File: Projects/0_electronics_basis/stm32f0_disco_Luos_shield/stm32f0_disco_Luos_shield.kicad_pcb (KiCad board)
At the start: 2 copper layers, 55.9 x 99.1 mm, 20 parts, among them J1 DF11-8DP-2DS(24), J2 DF11-8DP-2DS(24), J3 Header6Contacts, J4 Header6Contacts, J5 Discovery_Socket, J6 Header5Contacts, U1 ST3485ECDR

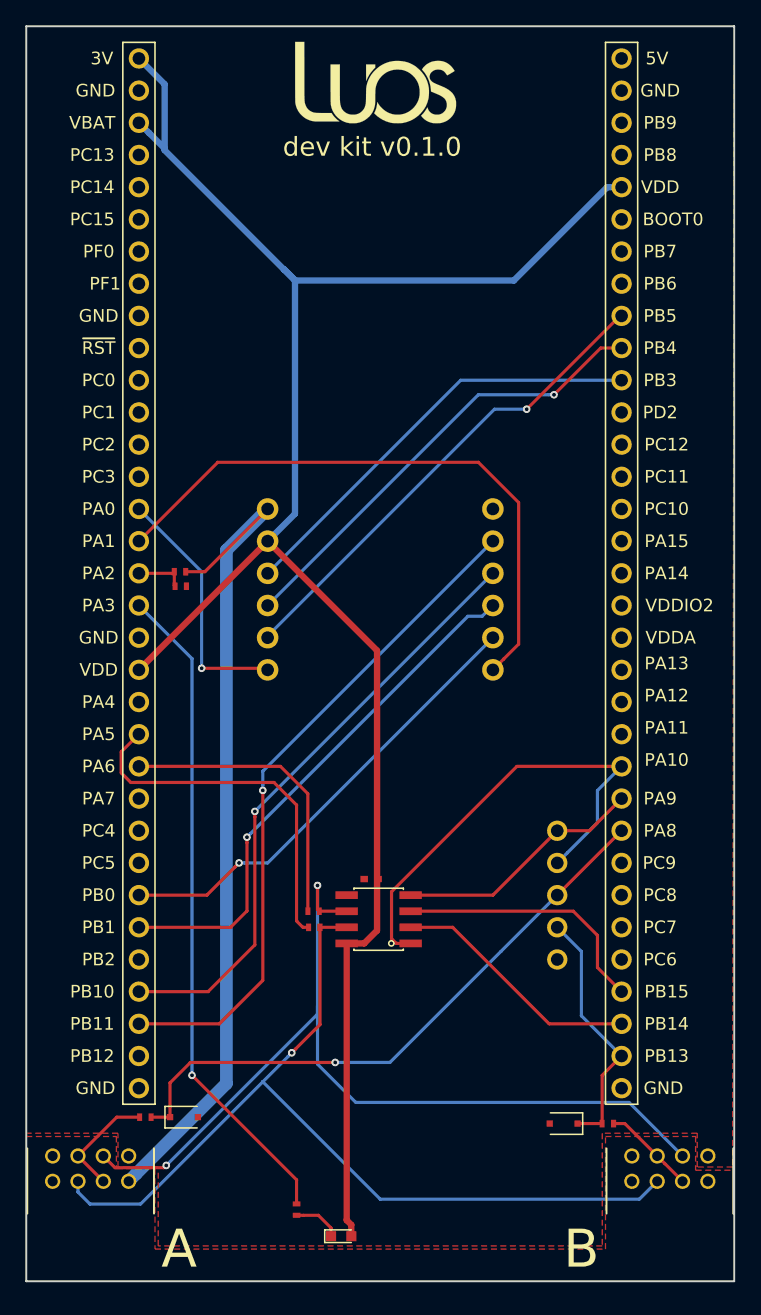
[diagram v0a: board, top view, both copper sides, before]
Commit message: change board kicad for project : Braekout board Luos Kit DC motor Servo
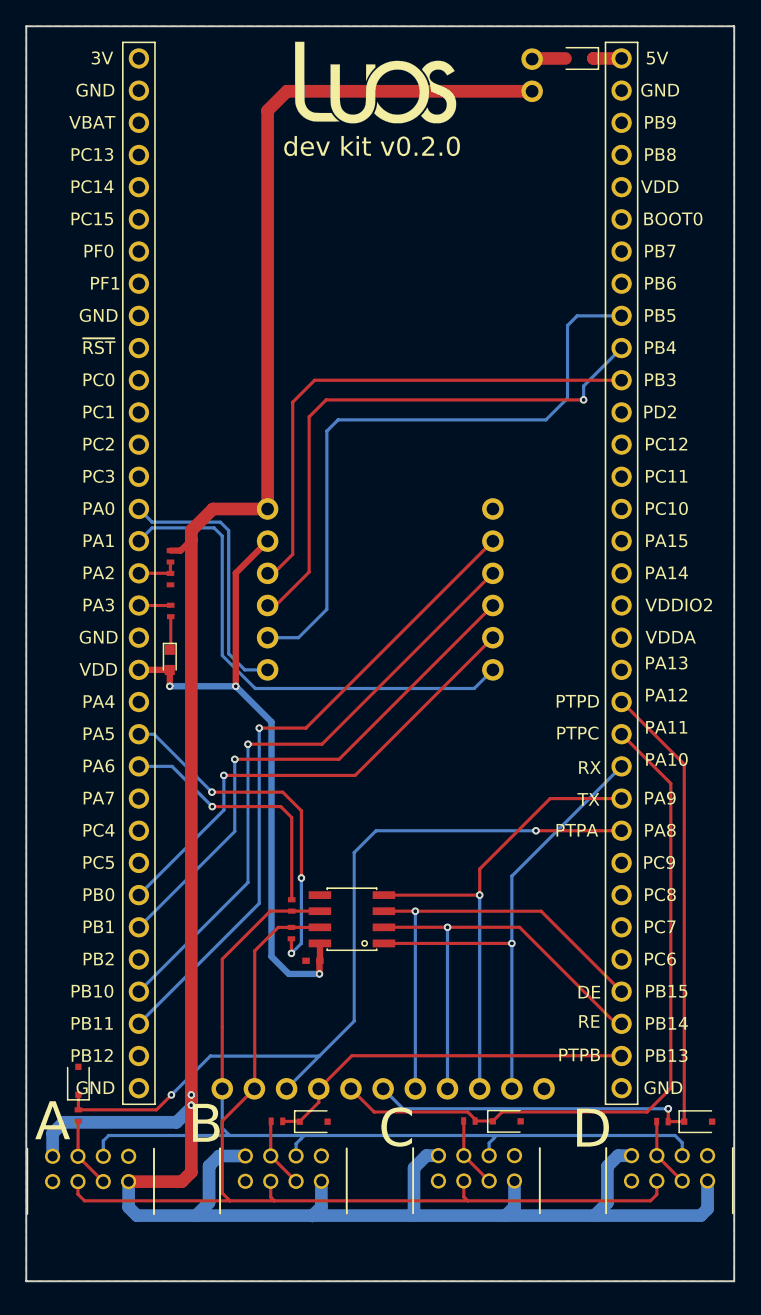
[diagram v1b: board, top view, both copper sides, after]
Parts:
- removed the D2 at (55.9, 111.7)
- removed the J5 at (41.4, 68.3)
- removed the J6 at (55.4, 93.7)
- added D1: D_Zener, Common_Footprint:D_SOD-323F, F.Cu at (17.6, 108.3)
- added D3: D_Zener, Common_Footprint:D_SOD-323F, F.Cu at (51.4, 111.5)
- added D4: D_Zener, Common_Footprint:D_SOD-323F, F.Cu at (66.5, 111.5)
- added D6: SMLE13BC8TT86, Common_Footprint:LED_0603, F.Cu at (24.8, 75.1)
- added J3: DF11-8DP-2DS(24), Common_Footprint:DF11-8DP-2DS(24), F.Cu at (49.0, 115.2)
- added J4: DF11-8DP-2DS, Common_Footprint:DF11-8DP-2DS(24), F.Cu at (64.3, 115.2)
- added J7: Discovery_Socket, Common_Footprint:Discovery_Socket, B.Cu at (41.4, 68.3)
- added J8: Header11Contacts, Common_Footprint:826926-11, B.Cu at (42.9, 109.0)
- added J9: Header2Contacts, Common_Footprint:826926-2, B.Cu at (53.4, 27.7)
- added R3: 100, Common_Footprint:R_0402_NoSilk, F.Cu at (48.5, 111.5)
- added R4: 100, Common_Footprint:R_0402_NoSilk, F.Cu at (63.7, 111.5)
- D5: value SMLE13BC8TT86 -> DIODE; footprint Common_Footprint:LED_0603 -> Common_Footprint:D_SOD-323F
- J1: value DF11-8DP-2DS(24) -> DF11-8DP-2DS
- moved D5 94.8 mm to (57.2, 27.6), turned to 180 degrees
- moved R9 48.3 mm to (24.9, 71.2)
- moved J1 45.7 mm to (18.6, 115.3)
- moved R1 41.8 mm to (17.6, 111.1), turned to 270 degrees
- moved J2 15.2 mm to (33.8, 115.3)
- moved R2 10.4 mm to (33.3, 111.5)
- moved D2 10.2 mm to (36.2, 111.5)
- moved C1 7.92 mm to (36.1, 98.8)
- moved U1 2.11 mm to (39.2, 95.6)
- moved R5 1.86 mm to (34.4, 96.7), turned to 90 degrees
- moved R6 1.78 mm to (34.5, 94.5), turned to 90 degrees
- moved R7 1.43 mm to (24.9, 66.9), turned to 90 degrees
- moved R8 0.99 mm to (24.9, 68.7), turned to 90 degrees
- renumbered C7 to C1, D3 to D2, J3 to J5, J4 to J6, R6 to R5, R7 to R6, R11 to R7, R12 to R8, R13 to R9
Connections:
- D2 pad 1: /PTPA -> /PTPB
- D5 pad 1: Net-(D5-Pad1) -> +5VP
- D5 pad 2: +3V3 -> Net-(D5-Pad2)
- J1 pad 3: /PTPB_PRO -> /PTPA_PRO
- J1 pad 6: /PTPB_PRO -> /PTPA_PRO
- J2 pad 3: /PTPA_PRO -> /PTPB_PRO
- J2 pad 6: /PTPA_PRO -> /PTPB_PRO
- R1 pad 1: /PTPB -> /PTPA
- R1 pad 2: /PTPB_PRO -> /PTPA_PRO
- R2 pad 1: /PTPA -> /PTPB
- R2 pad 2: /PTPA_PRO -> /PTPB_PRO
- R9 pad 1: Net-(D5-Pad1) -> Net-(D6-Pad1)
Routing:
- net /Vin: track 66.1 -> 208.9 mm, vias 0 -> 2
- net +3V3: track 151.8 -> 50.8 mm, vias 0 -> 3
- net /PTPD: track 0.00 -> 60.6 mm, vias 0 -> 1
- net /PTPC: track 0.00 -> 57.0 mm
- net Net-(J7-Pad49): track 52.4 -> 2.52 mm, vias 1 -> 0
- net /TxD: track 19.8 -> 38.4 mm, vias 0 -> 1
- net /PTPA: track 48.1 -> 64.7 mm, vias 1 -> 2
- net /RE: track 19.8 -> 34.7 mm, vias 0 -> 1
- net /DE: track 20.8 -> 35.4 mm, vias 0 -> 1
- net /MOSI/SD: track 38.5 -> 50.3 mm, vias 1 -> 0
- net /PTPB: track 20.2 -> 29.6 mm
- net /TIM2.2/ADC1: track 47.9 -> 39.8 mm
- net /MISO/MCK: track 36.4 -> 44.2 mm
- net /SCK/CK: track 34.3 -> 41.3 mm
- net /B_RS_485_P: track 71.6 -> 78.6 mm, vias 1 -> 0
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- removed copper zone on F.Cu, net /Vin
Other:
- net class ALIM added: clearance 0.508, trace_width 1, via_dia 0.6, via_drill 0.3
- board text added: "C"
- board text added: "D"
- board text added: "DE"
- board text added: "PTPC"
- board text added: "PTPD"
- board text added: "RE"
- board text added: "RX"
- board text added: "TX"
- board text added: "dev kit v0.2.0"
- board text removed: "dev kit v0.1.0"
